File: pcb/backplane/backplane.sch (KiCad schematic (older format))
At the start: 12 parts

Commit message: footprints
added footprints
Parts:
- added JST1, JST2, JST3, JST4: B4B-XH-A, backplane:B4B-XH-A, symbol backplane_Library:B4B-XH-A
- added Motor1Header1, Motor1Header2, Motor1Header3, Motor2Header1, Motor2Header2, Motor2Header3, Motor3Header1, Motor3Header2, Motor3Header3, Motor4Header1, Motor4Header2, Motor4Header3: PRPC006SAAN-RC, backplane:PRPC006SAAN-RC, symbol backplane_Library:PRPC006SAAN-RC
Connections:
- net labels added: Motor1EncoderPin1, Motor1EncoderPin2, Motor1EncoderPin3, Motor1EncoderPin4, Motor1EncoderPin5, Motor1EncoderPin6, Motor2EncoderPin1, Motor2EncoderPin2, Motor2EncoderPin3, Motor2EncoderPin4, Motor2EncoderPin5, Motor2EncoderPin6, Motor3EncoderPin1, Motor3EncoderPin2, Motor3EncoderPin3, Motor3EncoderPin4, Motor3EncoderPin5, Motor3EncoderPin6, Motor4EncoderPin1, Motor4EncoderPin2, Motor4EncoderPin3, Motor4EncoderPin4, Motor4EncoderPin5, Motor4EncoderPin6
- wire segments 49 -> 137

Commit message: updated pcb
added footprints and schematic
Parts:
- removed Motor1Header1, Motor1Header2, Motor1Header3, Motor2Header1, Motor2Header2, Motor2Header3, Motor3Header1, Motor3Header2, Motor3Header3, Motor4Header1, Motor4Header2, Motor4Header3: PRPC006SAAN-RC, backplane:PRPC006SAAN-RC, symbol backplane_Library:PRPC006SAAN-RC
- added JST5, JST6, JST7, JST8: B4B-XH-A, backplane:B4B-XH-A, symbol backplane_Library:B4B-XH-A
- added U1, U2, U3, U4: 74LVCH2T45DC,125, backplane:74LVCH2T45DC,125, symbol backplane_Library:74LVCH2T45DC,125
- added barrelJack1, barrelJack2, barrelJack3: PJ-037A, backplane:PJ-037A, symbol backplane_Library:PJ-037A
- added encoderpins1, encoderpins2, encoderpins3, encoderpins4, encoderpins5, encoderpins6, encoderpins7, encoderpins8: PREC002SAAN-RC, backplane:PREC002SAAN-RC, symbol backplane_Library:PREC002SAAN-RC
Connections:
- net labels added: +12V, +3.3V, +5V, Motor1EncoderA, Motor1EncoderA_3v3, Motor1EncoderB, Motor1EncoderB_3v3, Motor2EncoderA, Motor2EncoderA_3v3, Motor2EncoderB, Motor2EncoderB_3v3, Motor3EncoderA, Motor3EncoderA_3v3, Motor3EncoderB, Motor3EncoderB_3v3, Motor4EncoderA, Motor4EncoderA_3v3, Motor4EncoderB, Motor4EncoderB_3v3
- net labels removed: Motor1EncoderPin1, Motor1EncoderPin2, Motor1EncoderPin3, Motor1EncoderPin4, Motor1EncoderPin5, Motor1EncoderPin6, Motor2EncoderPin1, Motor2EncoderPin2, Motor2EncoderPin3, Motor2EncoderPin4, Motor2EncoderPin5, Motor2EncoderPin6, Motor3EncoderPin1, Motor3EncoderPin2, Motor3EncoderPin3, Motor3EncoderPin4, Motor3EncoderPin5, Motor3EncoderPin6, Motor4EncoderPin1, Motor4EncoderPin2, Motor4EncoderPin3, Motor4EncoderPin4, Motor4EncoderPin5, Motor4EncoderPin6
- wire segments 137 -> 158
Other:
- note added: "these connectors support andymark and builda motors"
- note added: "these connectors support textrix and rev motors"

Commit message: idk
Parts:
- JST1, JST2, JST3, JST4, JST5, JST6, JST7, JST8: symbol backplane_Library:B4B-XH-A -> backplane-rescue:B4B-XH-A-backplane_Library
- U1, U2, U3, U4: symbol backplane_Library:74LVCH2T45DC,125 -> backplane-rescue:74LVCH2T45DC,125-backplane_Library
- barrelJack1, barrelJack2, barrelJack3: symbol backplane_Library:PJ-037A -> backplane-rescue:PJ-037A-backplane_Library
- encoderpins1, encoderpins2, encoderpins3, encoderpins4, encoderpins5, encoderpins6, encoderpins7, encoderpins8: symbol backplane_Library:PREC002SAAN-RC -> backplane-rescue:PREC002SAAN-RC-backplane_Library
- lipo1Gnd1, lipo1Pwr1, lipo2Gnd1, lipo2Pwr1, motor1Gnd1, motor1Pwr1, motor2Gnd1, motor2Pwr1, motor3Gnd1, motor3Pwr1, motor4Gnd1, motor4Pwr1: symbol backplane_Library:CT3151V1-5 -> backplane-rescue:CT3151V1-5-backplane_Library
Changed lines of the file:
@@
 Connection ~ 1750 750
 $Comp
-L backplane_Library:CT3151V1-5 motor1Pwr1
+L backplane-rescue:CT3151V1-5-backplane_Library motor1Pwr1
 U 1 1 5C31259A
 P 1500 800
@@
 Connection ~ 1750 1200
 $Comp
-L backplane_Library:CT3151V1-5 motor2Pwr1
+L backplane-rescue:CT3151V1-5-backplane_Library motor2Pwr1
 U 1 1 5C312A1D
 P 1500 1250
@@
 Connection ~ 1750 1650
 $Comp
-L backplane_Library:CT3151V1-5 motor3Pwr1
+L backplane-rescue:CT3151V1-5-backplane_Library motor3Pwr1
 U 1 1 5C312A7A
 P 1500 1700
@@
 Connection ~ 1750 2100
 $Comp
-L backplane_Library:CT3151V1-5 motor4Pwr1
+L backplane-rescue:CT3151V1-5-backplane_Library motor4Pwr1
 U 1 1 5C312B34
 P 1500 2150
@@
 Connection ~ 3750 750
 $Comp
-L backplane_Library:CT3151V1-5 motor1Gnd1
+L backplane-rescue:CT3151V1-5-backplane_Library motor1Gnd1
 U 1 1 5C312D35
 P 3500 800
@@
 Connection ~ 3750 1200
 $Comp
-L backplane_Library:CT3151V1-5 motor2Gnd1
+L backplane-rescue:CT3151V1-5-backplane_Library motor2Gnd1
 U 1 1 5C312D44
 P 3500 1250
@@
 Connection ~ 3750 1650
 $Comp
-L backplane_Library:CT3151V1-5 motor3Gnd1
+L backplane-rescue:CT3151V1-5-backplane_Library motor3Gnd1
 U 1 1 5C312D53
 P 3500 1700
@@
 Connection ~ 3750 2100
 $Comp
-L backplane_Library:CT3151V1-5 motor4Gnd1
+L backplane-rescue:CT3151V1-5-backplane_Library motor4Gnd1
 U 1 1 5C312D62
 P 3500 2150
@@
 Connection ~ 1800 2900
 $Comp
-L backplane_Library:CT3151V1-5 lipo1Pwr1
+L backplane-rescue:CT3151V1-5-backplane_Library lipo1Pwr1
 U 1 1 5C313EC2
 P 1550 2950
@@
 Connection ~ 1800 3350
 $Comp
-L backplane_Library:CT3151V1-5 lipo2Pwr1
+L backplane-rescue:CT3151V1-5-backplane_Library lipo2Pwr1
 U 1 1 5C313ED1
 P 1550 3400
@@
 Connection ~ 3800 2900
 $Comp
-L backplane_Library:CT3151V1-5 lipo1Gnd1
+L backplane-rescue:CT3151V1-5-backplane_Library lipo1Gnd1
 U 1 1 5C313EDE
 P 3550 2950
@@
 Connection ~ 3800 3350
 $Comp
-L backplane_Library:CT3151V1-5 lipo2Gnd1
+L backplane-rescue:CT3151V1-5-backplane_Library lipo2Gnd1
 U 1 1 5C313EEB
 P 3550 3400
@@
 $EndComp
 $Comp
-L backplane_Library:B4B-XH-A JST1
+L backplane-rescue:B4B-XH-A-backplane_Library JST1
 U 1 1 5C3164AB
 P 5250 1000
@@
 $EndComp
 $Comp
-L backplane_Library:B4B-XH-A JST3
+L backplane-rescue:B4B-XH-A-backplane_Library JST3
 U 1 1 5C316566
 P 5200 2350
@@
 $EndComp
 $Comp
-L backplane_Library:B4B-XH-A JST2
+L backplane-rescue:B4B-XH-A-backplane_Library JST2
 U 1 1 5C3165D6
 P 6350 1000
@@
 $EndComp
 $Comp
-L backplane_Library:B4B-XH-A JST4
+L backplane-rescue:B4B-XH-A-backplane_Library JST4
 U 1 1 5C31675A
 P 6400 2350
@@
 	6300 2550 6350 2550
 $Comp
-L backplane_Library:B4B-XH-A JST5
+L backplane-rescue:B4B-XH-A-backplane_Library JST5
 U 1 1 5C37AFBA
 P 8650 2350
@@
 $EndComp
 $Comp
-L backplane_Library:B4B-XH-A JST7
+L backplane-rescue:B4B-XH-A-backplane_Library JST7
 U 1 1 5C37AFC1
 P 9800 1000
@@
 $EndComp
 $Comp
-L backplane_Library:B4B-XH-A JST8
+L backplane-rescue:B4B-XH-A-backplane_Library JST8
 U 1 1 5C37AFC8
 P 9850 2350
@@
 $EndComp
 $Comp
-L backplane_Library:B4B-XH-A JST6
+L backplane-rescue:B4B-XH-A-backplane_Library JST6
 U 1 1 5C37AFB3
 P 8700 1000
@@
 these connectors support textrix and rev motors
 $Comp
-L backplane_Library:PREC002SAAN-RC encoderpins1
+L backplane-rescue:PREC002SAAN-RC-backplane_Library encoderpins1
 U 1 1 5C4C6E55
 P 1050 4450
@@
 Motor1EncoderA
 $Comp
-L backplane_Library:PREC002SAAN-RC encoderpins5
+L backplane-rescue:PREC002SAAN-RC-backplane_Library encoderpins5
 U 1 1 5C4D0A4E
 P 1850 4450
@@
 	1000 4850 1000 4450
 $Comp
-L backplane_Library:PREC002SAAN-RC encoderpins2
+L backplane-rescue:PREC002SAAN-RC-backplane_Library encoderpins2
 U 1 1 5C4DF04F
 P 1050 6100
@@
 Motor3EncoderA
 $Comp
-L backplane_Library:PREC002SAAN-RC encoderpins6
+L backplane-rescue:PREC002SAAN-RC-backplane_Library encoderpins6
 U 1 1 5C4DF058
 P 1850 6100
@@
 	1000 6500 1000 6100
 $Comp
-L backplane_Library:PREC002SAAN-RC encoderpins3
+L backplane-rescue:PREC002SAAN-RC-backplane_Library encoderpins3
 U 1 1 5C4E1782
 P 2700 4450
@@
 Motor2EncoderA
 $Comp
-L backplane_Library:PREC002SAAN-RC encoderpins7
+L backplane-rescue:PREC002SAAN-RC-backplane_Library encoderpins7
 U 1 1 5C4E178B
 P 3500 4450
@@
 	2650 4850 2650 4450
 $Comp
-L backplane_Library:PREC002SAAN-RC encoderpins4
+L backplane-rescue:PREC002SAAN-RC-backplane_Library encoderpins4
 U 1 1 5C4E4309
 P 2750 6100
@@
 Motor4EncoderA
 $Comp
-L backplane_Library:PREC002SAAN-RC encoderpins8
+L backplane-rescue:PREC002SAAN-RC-backplane_Library encoderpins8
 U 1 1 5C4E4312
 P 3550 6100
@@
 	1100 4450 1100 4850
 $Comp
-L backplane_Library:74LVCH2T45DC,125 U1
+L backplane-rescue:74LVCH2T45DC,125-backplane_Library U1
 U 1 1 5C50CE3B
 P 5700 3950
@@
 	6150 4100 6100 4100
 $Comp
-L backplane_Library:74LVCH2T45DC,125 U3
+L backplane-rescue:74LVCH2T45DC,125-backplane_Library U3
 U 1 1 5C5469F9
 P 8500 3950
@@
 	8950 4100 8900 4100
 $Comp
-L backplane_Library:74LVCH2T45DC,125 U2
+L backplane-rescue:74LVCH2T45DC,125-backplane_Library U2
 U 1 1 5C54A97F
 P 5700 4950
@@
 	6150 5100 6100 5100
 $Comp
-L backplane_Library:74LVCH2T45DC,125 U4
+L backplane-rescue:74LVCH2T45DC,125-backplane_Library U4
 U 1 1 5C54F340
 P 8550 4950
@@
 	9000 5100 8950 5100
 $Comp
-L backplane_Library:PJ-037A barrelJack1
+L backplane-rescue:PJ-037A-backplane_Library barrelJack1
 U 1 1 5C55FED8
 P 4450 5950
@@
 $EndComp
 $Comp
-L backplane_Library:PJ-037A barrelJack2
+L backplane-rescue:PJ-037A-backplane_Library barrelJack2
 U 1 1 5C55FFE8
 P 5100 5950
@@
 $EndComp
 $Comp
-L backplane_Library:PJ-037A barrelJack3
+L backplane-rescue:PJ-037A-backplane_Library barrelJack3
 U 1 1 5C5600AC
 P 5750 5950

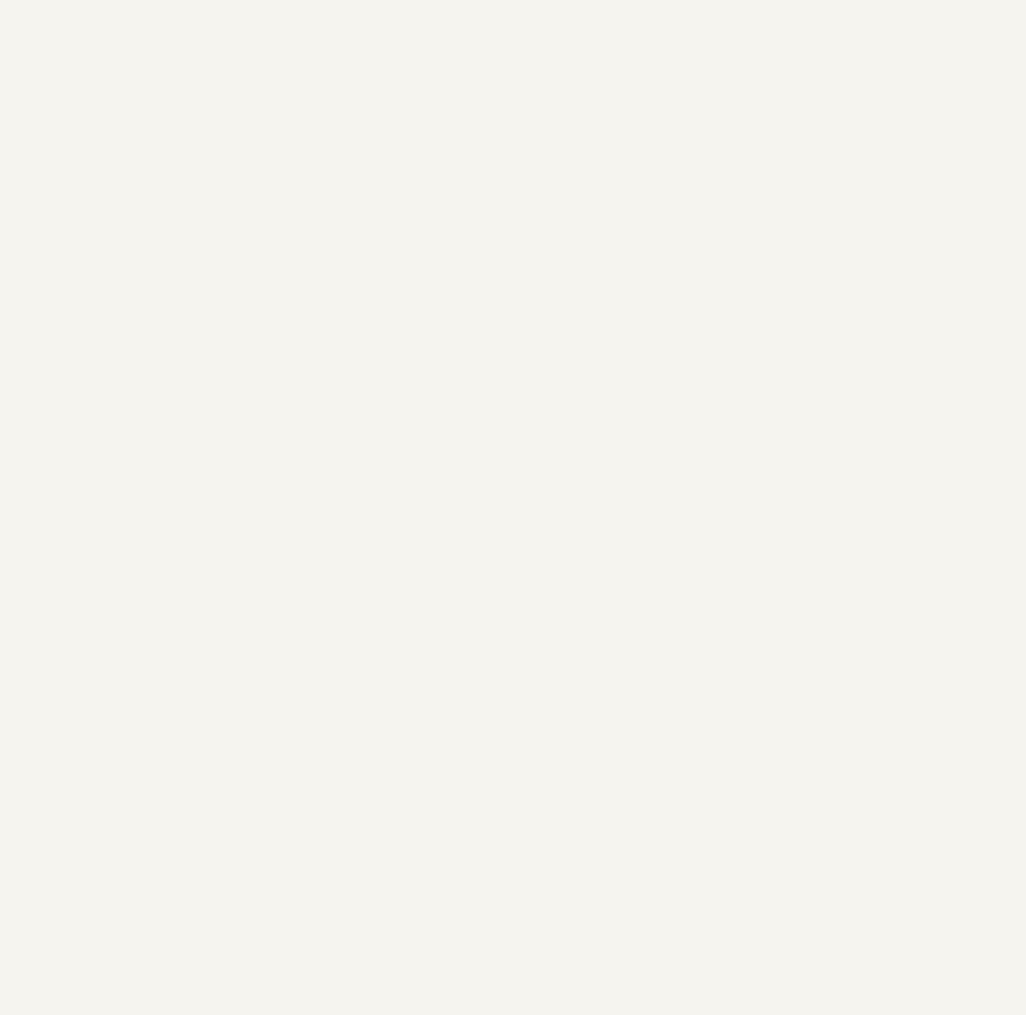
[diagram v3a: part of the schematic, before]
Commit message: updated footprints
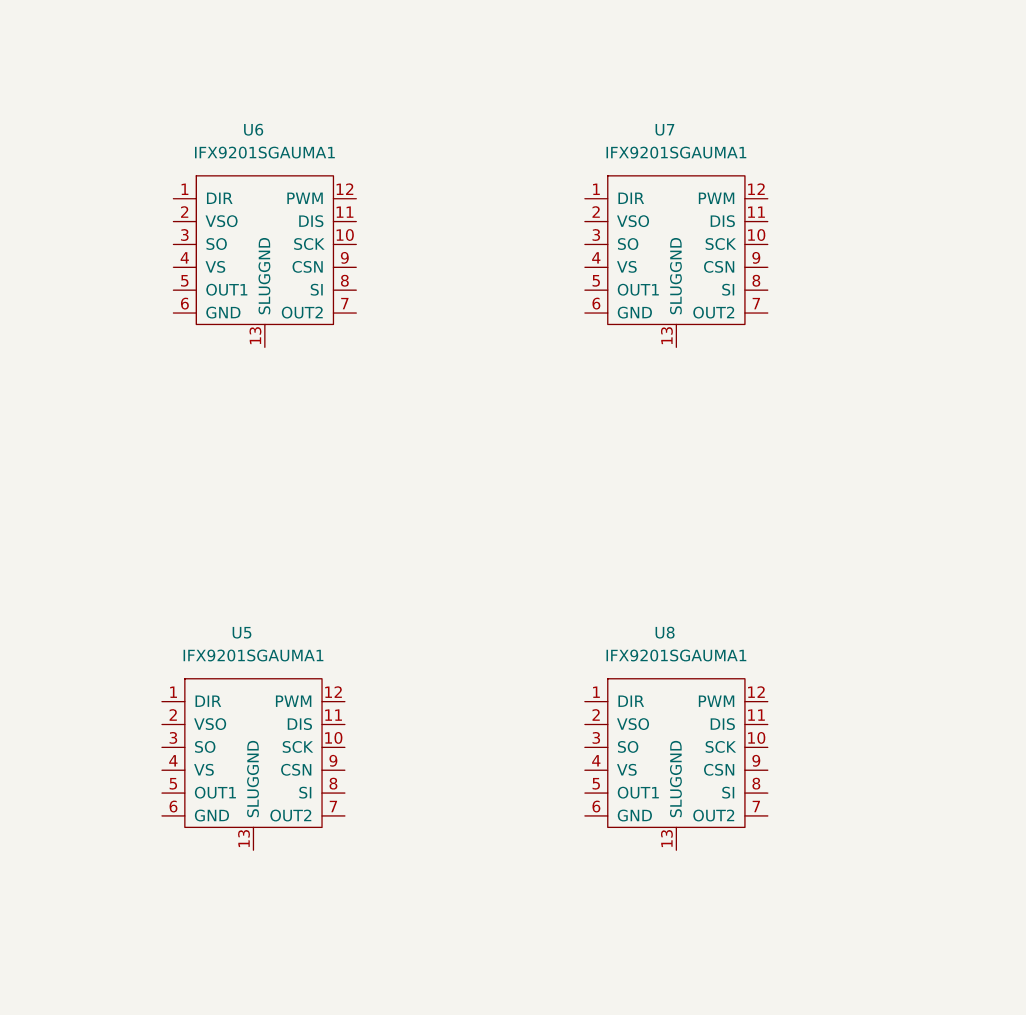
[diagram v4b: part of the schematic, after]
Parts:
- added U5, U6, U7, U8: IFX9201SGAUMA1, backplane:IFX9201SGAUMA1, symbol backplane_Library:IFX9201SGAUMA1
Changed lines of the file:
@@
 EELAYER 26 0
 EELAYER END
-$Descr A4 11693 8268
+$Descr A2 23386 16535
 encoding utf-8
 Sheet 1 1
@@
 Wire Wire Line
 	5950 6050 5950 6150
+$Comp
+L backplane_Library:IFX9201SGAUMA1 U6
+U 1 1 5C375057
+P 12450 1200
+F 0 "U6" H 12400 1700 50  0000 C CNN
+F 1 "IFX9201SGAUMA1" H 12450 1600 50  0000 C CNN
+F 2 "backplane:IFX9201SGAUMA1" H 12250 1200 50  0001 C CNN
+F 3 "" H 12250 1200 50  0001 C CNN
+	1    12450 1200
+	1    0    0    -1
+$EndComp
+$Comp
+L backplane_Library:IFX9201SGAUMA1 U7
+U 1 1 5C375322
+P 14250 1200
+F 0 "U7" H 14200 1700 50  0000 C CNN
+F 1 "IFX9201SGAUMA1" H 14250 1600 50  0000 C CNN
+F 2 "backplane:IFX9201SGAUMA1" H 14050 1200 50  0001 C CNN
+F 3 "" H 14050 1200 50  0001 C CNN
+	1    14250 1200
+	1    0    0    -1
+$EndComp
+$Comp
+L backplane_Library:IFX9201SGAUMA1 U5
+U 1 1 5C37B1D0
+P 12400 3400
+F 0 "U5" H 12350 3900 50  0000 C CNN
+F 1 "IFX9201SGAUMA1" H 12400 3800 50  0000 C CNN
+F 2 "backplane:IFX9201SGAUMA1" H 12200 3400 50  0001 C CNN
+F 3 "" H 12200 3400 50  0001 C CNN
+	1    12400 3400
+	1    0    0    -1
+$EndComp
+$Comp
+L backplane_Library:IFX9201SGAUMA1 U8
+U 1 1 5C381079
+P 14250 3400
+F 0 "U8" H 14200 3900 50  0000 C CNN
+F 1 "IFX9201SGAUMA1" H 14250 3800 50  0000 C CNN
+F 2 "backplane:IFX9201SGAUMA1" H 14050 3400 50  0001 C CNN
+F 3 "" H 14050 3400 50  0001 C CNN
+	1    14250 3400
+	1    0    0    -1
+$EndComp
 $EndSCHEMATC

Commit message: updates
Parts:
- removed lipo1Gnd1, lipo1Pwr1, lipo2Gnd1, lipo2Pwr1, motor1Gnd1, motor1Pwr1, motor2Gnd1, motor2Pwr1, motor3Gnd1, motor3Pwr1, motor4Gnd1, motor4Pwr1: CT3151V1-5, backplane:CT3151V1-5, symbol backplane-rescue:CT3151V1-5-backplane_Library
- added LipoGnd1, lipoGnd1, lipoIn1, lipoIn2, motorGnd1, motorGnd2, motorGnd3, motorGnd4, motorPwm1, motorPwm2, motorPwm3, motorPwm4: 1336G1, backplane:1336G1, symbol backplane_Library:1336G1
- added U1: PCA9685PW, Package_SO:TSSOP-28_4.4x9.7mm_P0.65mm, symbol Driver_LED:PCA9685PW
- added rail12v1, rail3v3, rail5v1: AP6503SP-13, backplane:AP6503SP-13, symbol backplane_Library:AP6503SP-13
- renumbered U1 to levelShift1, U3 to levelShift2, U2 to levelShift3, U4 to levelShift4
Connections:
- wire segments 158 -> 145

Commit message: updates
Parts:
- removed U5, U7, U8: IFX9201SGAUMA1, backplane:IFX9201SGAUMA1, symbol backplane_Library:IFX9201SGAUMA1
- added U?: PREC004SAAN-RC, symbol backplane_Library:PREC004SAAN-RC
- added U? (x3): IFX9201SGAUMA1, backplane:IFX9201SGAUMA1, symbol backplane_Library:IFX9201SGAUMA1
- added motorControl1, motorControl2, motorControl3, motorControl?: PREC002SAAN-RC, backplane:PREC002SAAN-RC, symbol backplane-rescue:PREC002SAAN-RC-backplane_Library
- renumbered motorPwm1 to motorControlOut1, motorPwm2 to motorControlOut2, motorPwm3 to motorControlOut3
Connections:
- net motor1PwmOut is gone; now on net motorControlOut1: motorControlOut1.1 (A)
- net +14v8: now also U6.4 (VS), U?.4 (VS), U?.4 (VS), U?.4 (VS)
- net +3V3: now also U6.2 (VSO), U?.2 (VSO), U?.2 (VSO), U?.2 (VSO)
- net GND: now also U6.11 (DIS), U6.13 (SLUGGND), U6.6 (GND), U?.11 (DIS), U?.11 (DIS), U?.11 (DIS), U?.13 (SLUGGND), U?.13 (SLUGGND), U?.13 (SLUGGND), U?.6 (GND), U?.6 (GND), U?.6 (GND)
- net motorDir1: now reaches U6.1 (DIR)
- net motorDir1: now also motorControl1.1 (A)
- net SCK: now reaches U6.10 (SCK)
- net SCK: now also U?.10 (SCK), U?.10 (SCK), U?.10 (SCK), U?.4 (D)
- net motorPwm1: now reaches U6.12 (PWM)
- net motorPwm1: now also motorControl1.2 (B)
- net SO1: now reaches U6.3 (SO)
- net SO1: now also U?.8 (SI)
- net motorControlOut1: now reaches U6.5 (OUT1)
- net motorGnd1: now reaches U6.7 (OUT2)
- net mcuSI: now reaches U6.8 (SI)
- net mcuSI: now also U?.2 (B)
- net CSN: now reaches U6.9 (CSN)
- net CSN: now also U?.3 (C), U?.9 (CSN), U?.9 (CSN), U?.9 (CSN)
- net motorControlOut3: now reaches motorControlOut3.1 (A)
- net motorControlOut3: now also U?.5 (OUT1)
- net motor2PwmOut renamed motorControlOut2
- net motorControlOut2: now also U?.5 (OUT1)
- net motor4PwmOut renamed motorControlOut4
- net motorControlOut4: now also U?.5 (OUT1)
- new net SO2: U?.3 (SO), U?.8 (SI)
- new net SO3: U?.3 (SO), U?.8 (SI)
- new net mcuSO: U?.1 (A), U?.3 (SO)
- new net motorDir2: U?.1 (DIR), motorControl2.1 (A)
- new net motorDir3: U?.1 (DIR), motorControl3.1 (A)
- new net motorDir4: U?.1 (DIR), motorControl?.1 (A)
- new net motorGnd2: U?.7 (OUT2)
- new net motorGnd3: U?.7 (OUT2)
- new net motorGnd4: U?.7 (OUT2)
- new net motorPwm2: U?.12 (PWM), motorControl2.2 (B)
- new net motorPwm3: U?.12 (PWM), motorControl3.2 (B)
- new net motorPwm4: U?.12 (PWM), motorControl?.2 (B)
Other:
- moved on the sheet: U6, motorControlOut1, motorControlOut2, motorControlOut3, motorGnd1, motorGnd2, motorGnd3, motorGnd4, motorPwm4

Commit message: updates
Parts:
- added C1, C2, C3, C4: 100uF, backplane:865080445010, symbol Device:CP
- added C5, C6, C7, C8: 100nF, backplane:865090640001, symbol Device:CP
- U5: renamed from U?; footprint (none) -> backplane:PREC004SAAN-RC
- gave numbers to parts that had none: 4
- renumbered motorPwm4 to motorControlOut4
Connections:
- net +14v8: now also C1.1, C2.1, C3.1, C4.1, C5.1, C6.1, C7.1, C8.1
- net GND: now also C1.2, C2.2, C3.2, C4.2, C5.2, C6.2, C7.2, C8.2; no longer motorGnd1.1 (A), motorGnd2.1 (A), motorGnd3.1 (A), motorGnd4.1 (A)
- net motorGnd1: now also motorGnd1.1 (A)
- net motorGnd2: now also motorGnd2.1 (A)
- net motorGnd3: now also motorGnd3.1 (A)
- net motorGnd4: now also motorGnd4.1 (A)
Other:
- moved on the sheet: U2, U3, U4, U6

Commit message: updates
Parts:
- removed U1: PCA9685PW, Package_SO:TSSOP-28_4.4x9.7mm_P0.65mm, symbol Driver_LED:PCA9685PW
- removed rail5v1: AP6503SP-13, backplane:AP6503SP-13, symbol backplane_Library:AP6503SP-13
- added C10, C16, C17: 47uF, backplane:865090449007, symbol Device:CP
- added C11, C18, C19: 10nF, Capacitor_SMD:C_1206_3216Metric_Pad1.42x1.75mm_HandSolder, symbol Device:CP
- added C12, C20, C22: 100nF, Capacitor_SMD:C_1206_3216Metric_Pad1.42x1.75mm_HandSolder, symbol Device:CP
- added C13, C21, C23: 6.8nF, Capacitor_SMD:C_1206_3216Metric_Pad1.42x1.75mm_HandSolder, symbol Device:CP
- added C14, C15, C9: 22uF, backplane:865090442004, symbol Device:CP
- added L1, L2, L3: 11uH, backplane:P0847SNL, symbol pspice:INDUCTOR
- added R1: 45.3K, Resistor_SMD:R_1206_3216Metric_Pad1.42x1.75mm_HandSolder, symbol Device:R
- added R10, R3, R9: 6.8k, Resistor_SMD:R_1206_3216Metric_Pad1.42x1.75mm_HandSolder, symbol Device:R
- added R11, R12, R4: 100K, Resistor_SMD:R_1206_3216Metric_Pad1.42x1.75mm_HandSolder, symbol Device:R
- added R2, R6, R8: 10K, Resistor_SMD:R_1206_3216Metric_Pad1.42x1.75mm_HandSolder, symbol Device:R
- added R5: 120K, Resistor_SMD:R_1206_3216Metric_Pad1.42x1.75mm_HandSolder, symbol Device:R
- added R7: 26.1K, Resistor_SMD:R_1206_3216Metric_Pad1.42x1.75mm_HandSolder, symbol Device:R
- added rail3v3: AP6503SP-13, backplane:AP6503SP-13, symbol backplane_Library:AP6503SP-13
- C5, C6, C7, C8: footprint backplane:865090640001 -> Capacitor_SMD:C_1206_3216Metric_Pad1.42x1.75mm_HandSolder
- renumbered rail3v3 to rail5v1
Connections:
- net +12V: now also C16.1, L2.1, R5.1
- net +14v8: now also rail12v1.2 (IN), rail5v1.2 (IN), C14.1, C15.1, C9.1, R11.1, R12.1, R4.1, rail3v3.2 (IN)
- net +3V3: now also C17.1, L3.1, R7.1
- net +5V: now also C10.1, L1.1, R1.1
- net GND: now also rail12v1.4 (GND), rail12v1.9 (GND), rail5v1.4 (GND), rail5v1.9 (GND), C10.2, C12.2, C14.2, C15.2, C16.2, C17.2, C20.2, C22.2, C9.2, R10.2, R2.2, R3.2, R6.2, R8.2, R9.2, rail3v3.4 (GND), rail3v3.9 (GND)
- net at rail5v1.1 (BST): now also C11.2
- net at rail5v1.3 (SW): now also C11.1, L1.2
- net at rail5v1.5 (FB): now also R1.2, R2.1
- net at rail5v1.6 (COMP): now also C13.1
- net at rail5v1.7 (EN): now also R4.2
- net at rail5v1.8 (SS): now also C12.1
- net at rail12v1.1 (BST): now also C18.2
- net at rail12v1.3 (SW): now also C18.1, L2.2
- net at rail12v1.5 (FB): now also R5.2, R6.1
- net at rail12v1.6 (COMP): now also C21.1
- net at rail12v1.7 (EN): now also R11.2
- net at rail12v1.8 (SS): now also C20.1
- new net: C13.2, R3.1
- new net: C19.2, rail3v3.1 (BST)
- new net: C19.1, L3.2, rail3v3.3 (SW)
- new net: R7.2, R8.1, rail3v3.5 (FB)
- new net: C23.1, rail3v3.6 (COMP)
- new net: R12.2, rail3v3.7 (EN)
- new net: C22.1, rail3v3.8 (SS)
- new net: C23.2, R10.1
- new net: C21.2, R9.1
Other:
- moved on the sheet: rail5v1
